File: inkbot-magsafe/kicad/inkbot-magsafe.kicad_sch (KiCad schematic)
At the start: 73 parts, among them J1 GDEM0397T81P panel FPC, J2 Protected battery + NTC, J3 WR222230 coil + bonded NTC, Q1 Si1308EDL-T1-GE3, U1 MDBT50Q-512K, U2 BQ51013C, U3 BQ25185DLHR, U4 TPS7A2030PDBVR, Y1 FC-135 32.768kHz 12.5pF

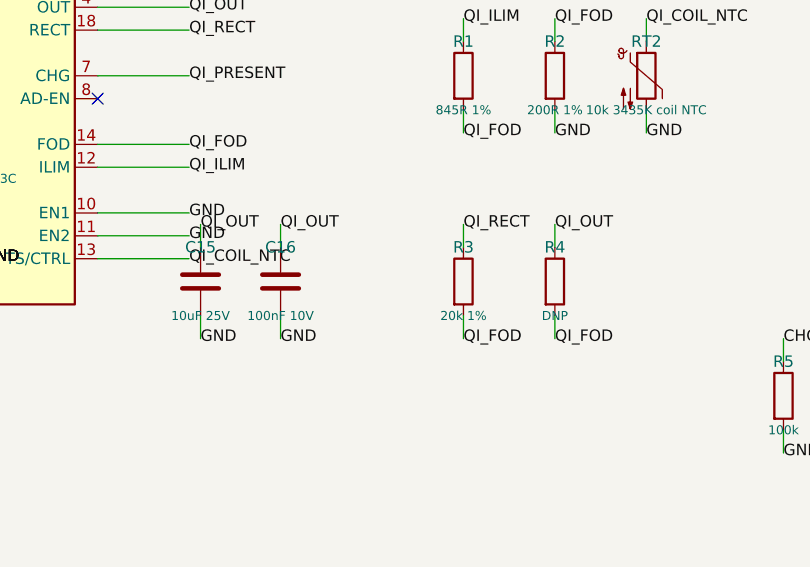
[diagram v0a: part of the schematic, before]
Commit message: inkbot-magsafe: align fabrication metadata
Co-authored-by: Jason Hall <imjasonh@users.noreply.github.com>
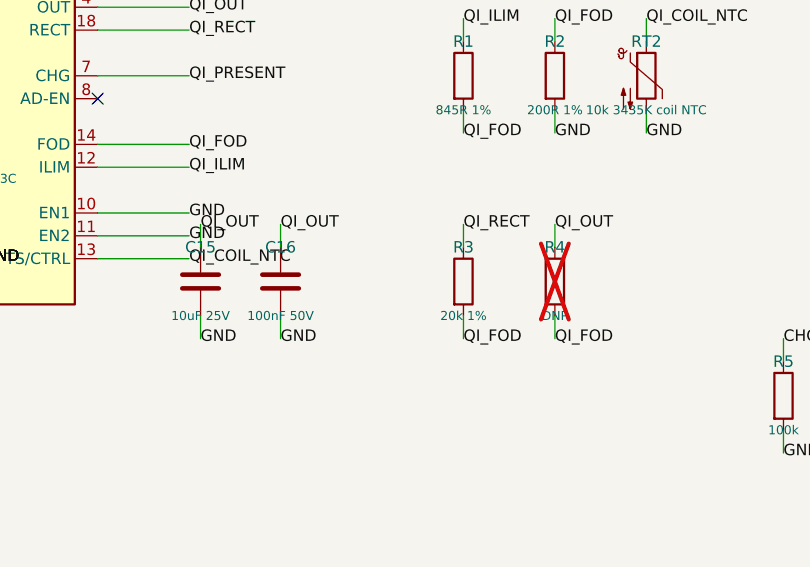
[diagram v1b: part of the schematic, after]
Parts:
- C16: value 100nF 10V -> 100nF 50V
- L1: footprint Inductor_SMD:L_TDK_NLV25_2.5x2.0mm -> inkbot_magsafe:TDK_VLS252010CX
- R4: now not fitted
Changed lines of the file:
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@@
     (property "Reference" "C16" (at 124.46 83.82 0)
       (effects (font (size 1.27 1.27))))
-    (property "Value" "100nF 10V" (at 124.46 91.44 0)
+    (property "Value" "100nF 50V" (at 124.46 91.44 0)
       (effects (font (size 1.0 1.0))))
     (property "Footprint" "Capacitor_SMD:C_0603_1608Metric" (at 124.46 92.71 0)
@@
   )
   (symbol (lib_id "Device:R") (at 154.94 87.63 0)
+    (dnp yes)
     (property "Reference" "R4" (at 154.94 83.82 0)
       (effects (font (size 1.27 1.27))))
@@
     (property "Value" "VLS252010CX-100M-1 10uH" (at 320.04 128.27 0)
       (effects (font (size 1.0 1.0))))
-    (property "Footprint" "Inductor_SMD:L_TDK_NLV25_2.5x2.0mm" (at 320.04 129.54 0)
+    (property "Footprint" "inkbot_magsafe:TDK_VLS252010CX" (at 320.04 129.54 0)
       (effects (font (size 1.27 1.27)) hide))
     (property "LCSC" "" (at 320.04 130.81 0)

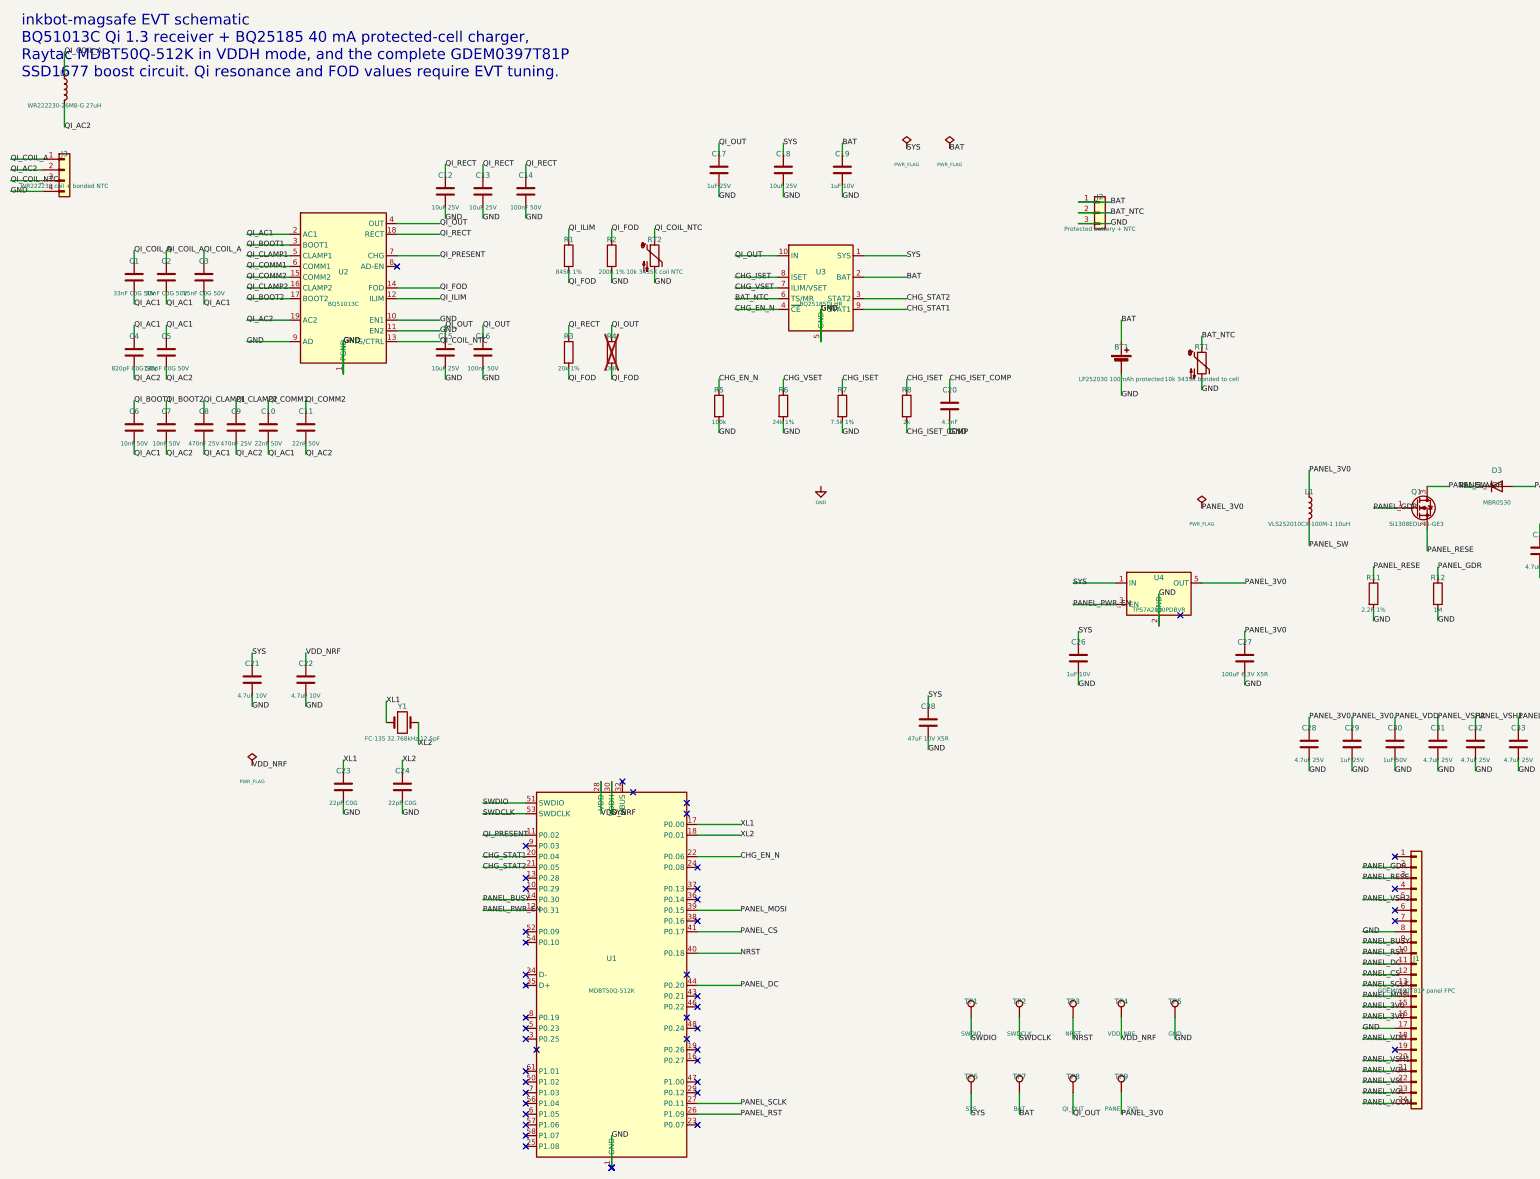
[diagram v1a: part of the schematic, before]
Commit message: inkbot-magsafe: fail closed on battery charging
Co-authored-by: Jason Hall <imjasonh@users.noreply.github.com>
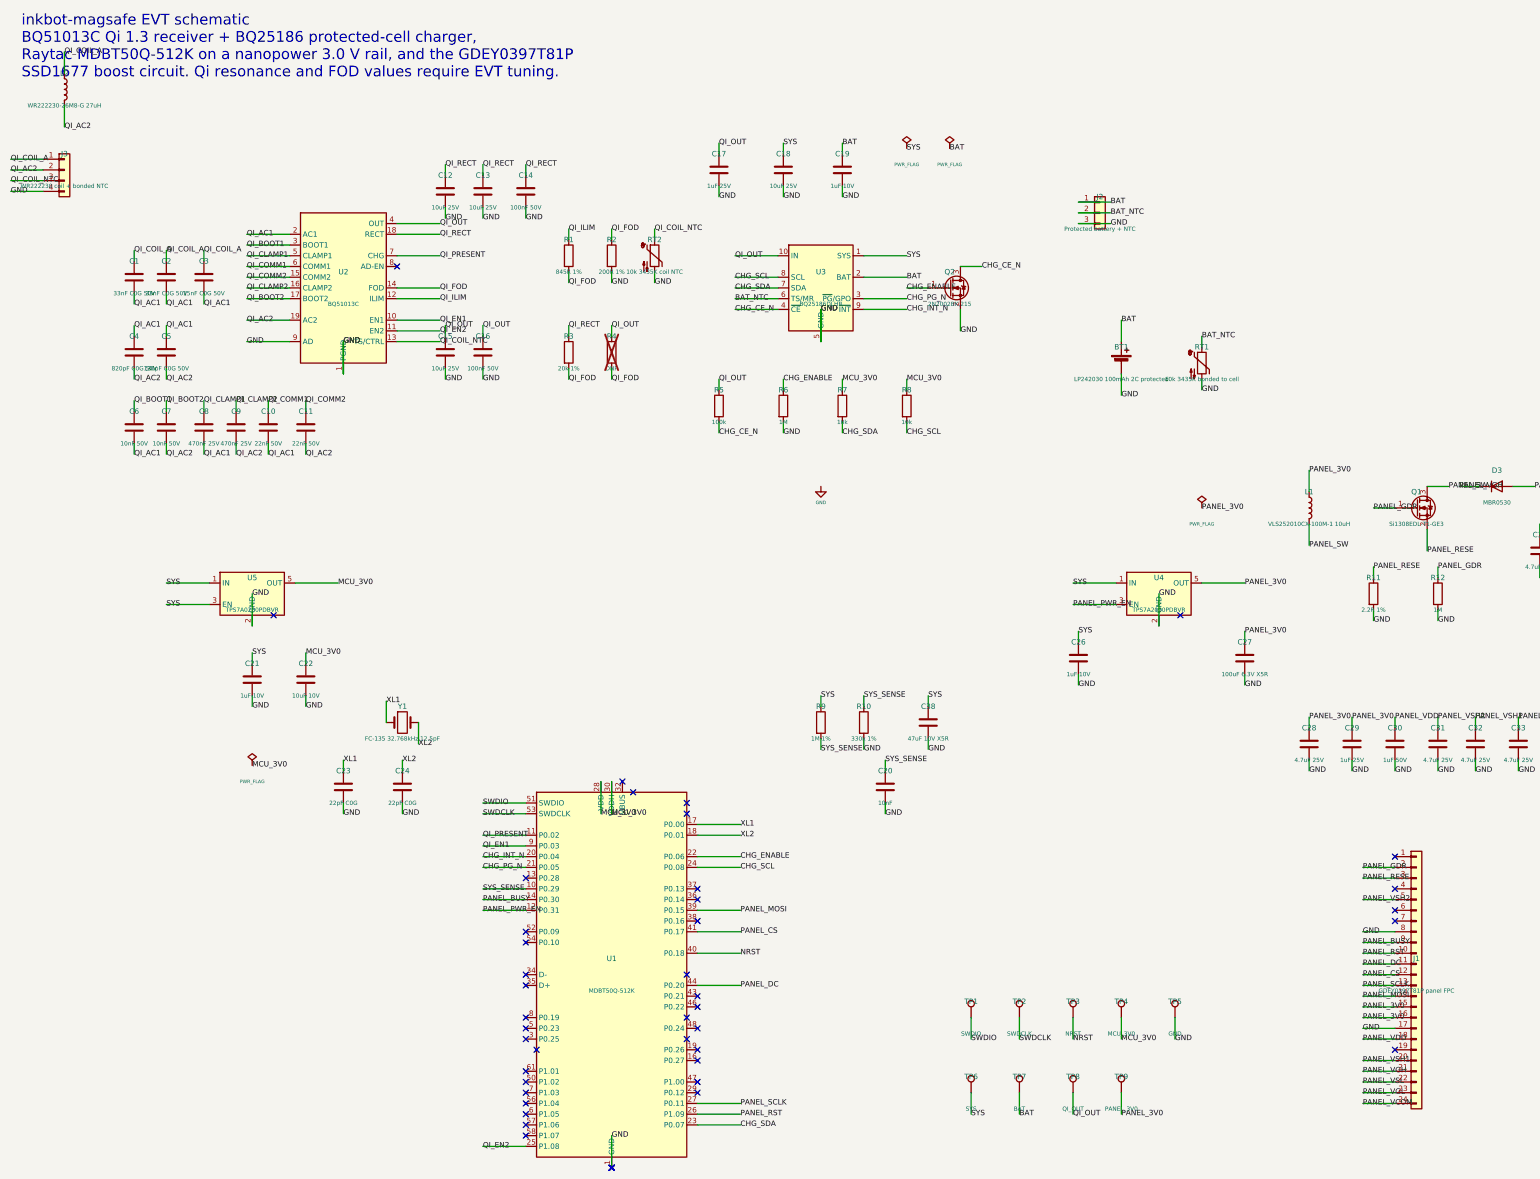
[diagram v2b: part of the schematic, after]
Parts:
- removed C33, C34, C35: 4.7uF 25V, Capacitor_SMD:C_0805_2012Metric, symbol Device:C
- removed C36: 1uF 50V, Capacitor_SMD:C_0603_1608Metric, symbol Device:C
- removed L1: VLS252010CX-100M-1 10uH, inkbot_magsafe:TDK_VLS252010CX, symbol Device:L
- removed Q1: Si1308EDL-T1-GE3, Package_TO_SOT_SMD:SOT-323_SC-70, symbol Device:Q_NMOS_GSD
- added C20: 10nF, Capacitor_SMD:C_0603_1608Metric, symbol Device:C
- added C37: 4.7uF 25V, Capacitor_SMD:C_0805_2012Metric, symbol Device:C
- added D1, D2: MBR0530, Diode_SMD:D_SOD-123, symbol Device:D
- added R10: 330k 1%, Resistor_SMD:R_0603_1608Metric, symbol Device:R
- added R11: 2.2R 1%, Resistor_SMD:R_0603_1608Metric, symbol Device:R
- added R12: 1M, Resistor_SMD:R_0603_1608Metric, symbol Device:R
- added R9: 1M 1%, Resistor_SMD:R_0603_1608Metric, symbol Device:R
- added TP5: GND, TestPoint:TestPoint_Pad_D1.0mm, symbol Connector:TestPoint
- added U5: TPS7A0230PDBVR, Package_TO_SOT_SMD:SOT-23-5, symbol inkbot_magsafe:TPS7A0230P
- BT1: value LP252030 100mAh protected -> LP242030 100mAh 2C protected
- C21: value 4.7uF 10V -> 1uF 10V
- C22: value 4.7uF 10V -> 10uF 10V; footprint Capacitor_SMD:C_0603_1608Metric -> Capacitor_SMD:C_0805_2012Metric
- C33: renamed from R11; value 2.2R 1% -> 4.7uF 25V; footprint Resistor_SMD:R_0603_1608Metric -> Capacitor_SMD:C_0805_2012Metric; symbol Device:R -> Device:C
- C34: renamed from R12; value 1M -> 4.7uF 25V; footprint Resistor_SMD:R_0603_1608Metric -> Capacitor_SMD:C_0805_2012Metric; symbol Device:R -> Device:C
- C35: renamed from D3; value MBR0530 -> 4.7uF 25V; footprint Diode_SMD:D_SOD-123 -> Capacitor_SMD:C_0805_2012Metric; symbol Device:D -> Device:C
- C36: renamed from C37; value 4.7uF 25V -> 1uF 50V; footprint Capacitor_SMD:C_0805_2012Metric -> Capacitor_SMD:C_0603_1608Metric
- D3: renamed from TP5; value GND -> MBR0530; footprint TestPoint:TestPoint_Pad_D1.0mm -> Diode_SMD:D_SOD-123; symbol Connector:TestPoint -> Device:D
- J1: value GDEM0397T81P panel FPC -> GDEY0397T81P panel FPC
- L1: renamed from D2; value MBR0530 -> VLS252010CX-100M-1 10uH; footprint Diode_SMD:D_SOD-123 -> inkbot_magsafe:TDK_VLS252010CX; symbol Device:D -> Device:L
- Q1: renamed from D1; value MBR0530 -> Si1308EDL-T1-GE3; footprint Diode_SMD:D_SOD-123 -> Package_TO_SOT_SMD:SOT-323_SC-70; symbol Device:D -> Device:Q_NMOS_GSD
- Q2: renamed from C20; value 4.7nF -> 2N7002BK,215; footprint Capacitor_SMD:C_0603_1608Metric -> Package_TO_SOT_SMD:SOT-23; symbol Device:C -> Device:Q_NMOS_GSD
- R6: value 24k 1% -> 1M
- R7: value 7.5k 1% -> 10k
- R8: value 2k -> 10k
- TP4: value VDD_NRF -> MCU_3V0
- U3: value BQ25185DLHR -> BQ25186DLHR; footprint inkbot_magsafe:BQ25185_DLH0010A -> inkbot_magsafe:TI_DLH0010A_WSON-10; symbol inkbot_magsafe:BQ25185 -> inkbot_magsafe:BQ25186
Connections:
- net VDD_NRF is gone; now on net MCU_3V0: C22.1, TP4.1, U1.28 (VDD)
- net EP: now also C35.2, C36.2, C20.2, D2.1 (K), R10.2, R11.2, R12.2, TP5.1, U5.2 (GND); no longer D3.1, L1.1 (K), R5.2, R7.2, U2.10 (EN1), U2.11 (EN2)
- net PANEL_3V0: now also L1.1
- net PANEL_GDR: now also Q1.1 (G), R12.1; no longer C34.1
- net PANEL_PUMP: now also C37.2, D1.1 (K), D2.2 (A); no longer C36.2, L1.2 (A), Q1.1 (K)
- net PANEL_RESE: now also Q1.2 (S), R11.1; no longer C33.1
- net PANEL_SW: now also D3.2 (A), L1.2, Q1.3 (D), C37.1; no longer C35.2 (A), C36.1
- net PANEL_VCOM: now also C36.1
- net PANEL_VGH: now also C33.1, D3.1 (K); no longer C35.1 (K)
- net PANEL_VGL: now also C35.1, D1.2 (A); no longer Q1.2 (A)
- net PANEL_VSL: now also C34.1
- net QI_OUT: now also R5.1
- net SYS: now also R9.1, U5.1 (IN), U5.3 (EN); no longer U1.30 (VDDH)
- net SYS_SENSE: now reaches U1.10 (P0.29)
- net SYS_SENSE: now also C20.1, R10.1, R9.2
- net CHG_SDA: now reaches U1.23 (P0.07)
- net CHG_SDA: now also R7.2, U3.7 (SDA)
- net CHG_SCL: now reaches U1.24 (P0.08)
- net CHG_SCL: now also R8.2, U3.8 (SCL)
- net QI_EN2: now reaches U1.25 (P1.08)
- net QI_EN2: now also U2.11 (EN2)
- net QI_EN1: now reaches U1.9 (P0.03)
- net QI_EN1: now also U2.10 (EN1)
- removed net CHG_EN_N: R5.1, U1.22 (P0.06), U3.4 (~{CE})
- net CHG_ISET renamed MCU_3V0
- net MCU_3V0: now also U1.30 (VDDH), U5.5 (OUT); no longer U3.8 (ISET)
- net CHG_ISET_COMP renamed CHG_ENABLE
- net CHG_ENABLE: now also R6.1, U1.22 (P0.06); no longer R8.2
- net CHG_STAT1 renamed CHG_INT_N
- net CHG_STAT2 renamed CHG_PG_N
- removed net CHG_VSET: R6.1, U3.7 (ILIM/VSET)
- new net CHG_CE_N: Q2.3 (D), R5.2, U3.4 (~{CE})
- no-connect marks 49 -> 45
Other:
- note added: "inkbot-magsafe EVT schematic BQ51013C Qi 1.3 receiver + BQ25186 protected-cell charger, Raytac MDBT50Q-512K on a nanopower 3.0 V rail, and the GDEY0397T81P SSD1677 boost circuit. Qi resonance and FOD values require EVT tuning."
- note removed: "inkbot-magsafe EVT schematic BQ51013C Qi 1.3 receiver + BQ25185 40 mA protected-cell charger, Raytac MDBT50Q-512K in VDDH mode, and the complete GDEM0397T81P SSD1677 boost circuit. Qi resonance and FOD values require EVT tuning."
- moved on the sheet: C36

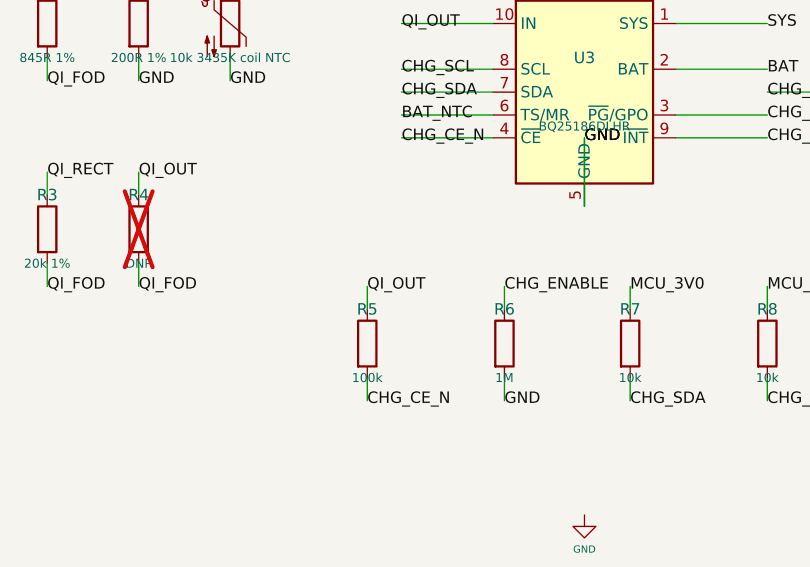
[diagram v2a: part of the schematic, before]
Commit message: inkbot-magsafe: hold charger off from battery rail
Co-authored-by: Jason Hall <imjasonh@users.noreply.github.com>
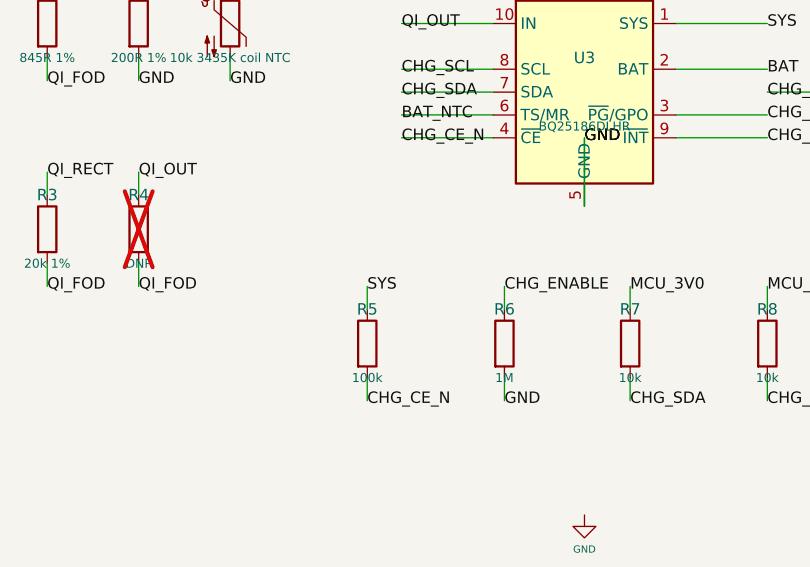
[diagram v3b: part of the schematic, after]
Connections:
- net QI_OUT: no longer R5.1
- net SYS: now also R5.1
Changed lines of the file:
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@@
     (effects (font (size 1.27 1.27)) (justify left))
   )
-  (label "QI_OUT" (at 180.34 93.98 0)
+  (label "SYS" (at 180.34 93.98 0)
     (effects (font (size 1.27 1.27)) (justify left))
   )
